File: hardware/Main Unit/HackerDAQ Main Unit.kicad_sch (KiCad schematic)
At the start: 10 parts, among them X2 8.192MHz

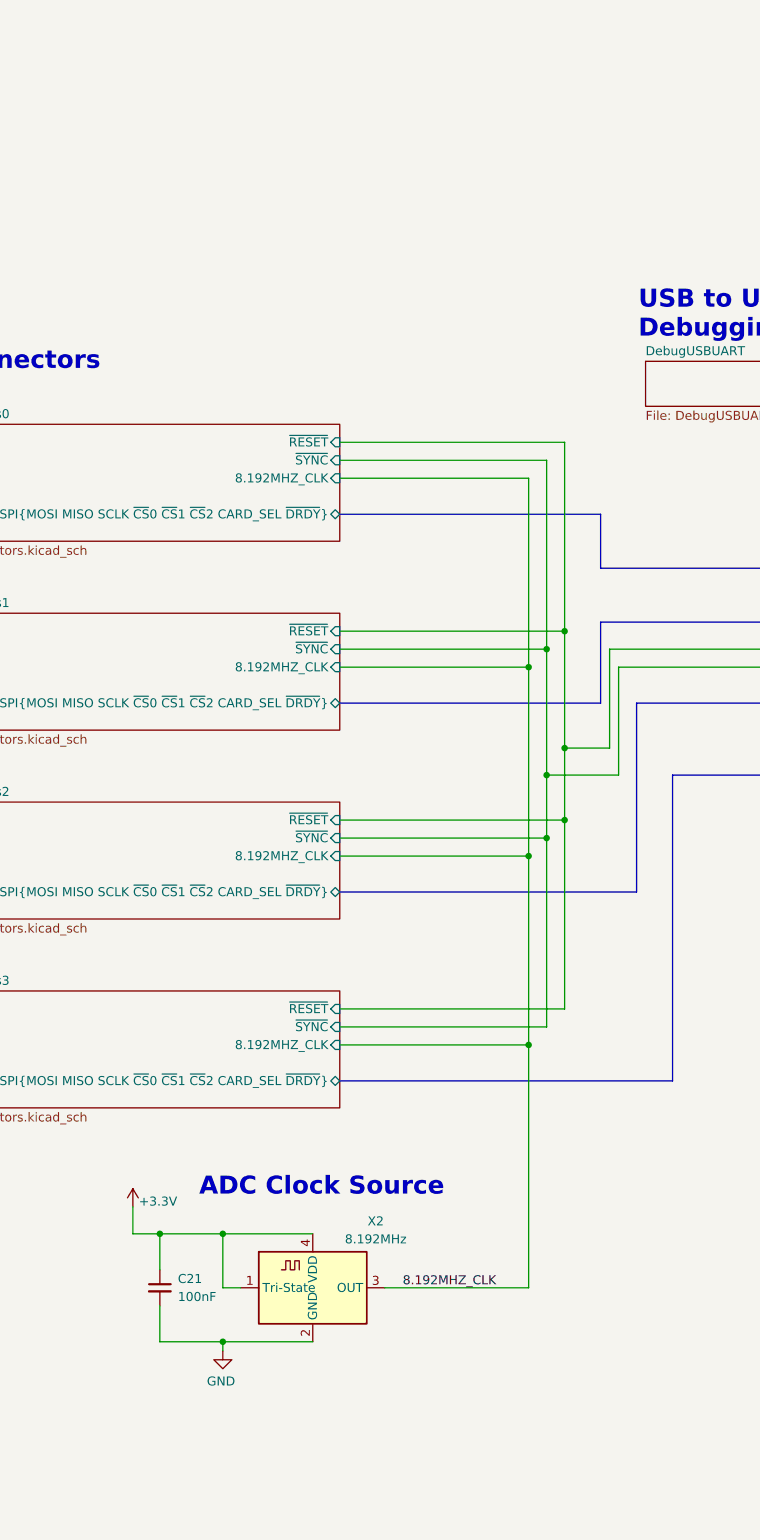
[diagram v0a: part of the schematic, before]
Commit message: Update main unit to KiCAD 10, add clock buffer
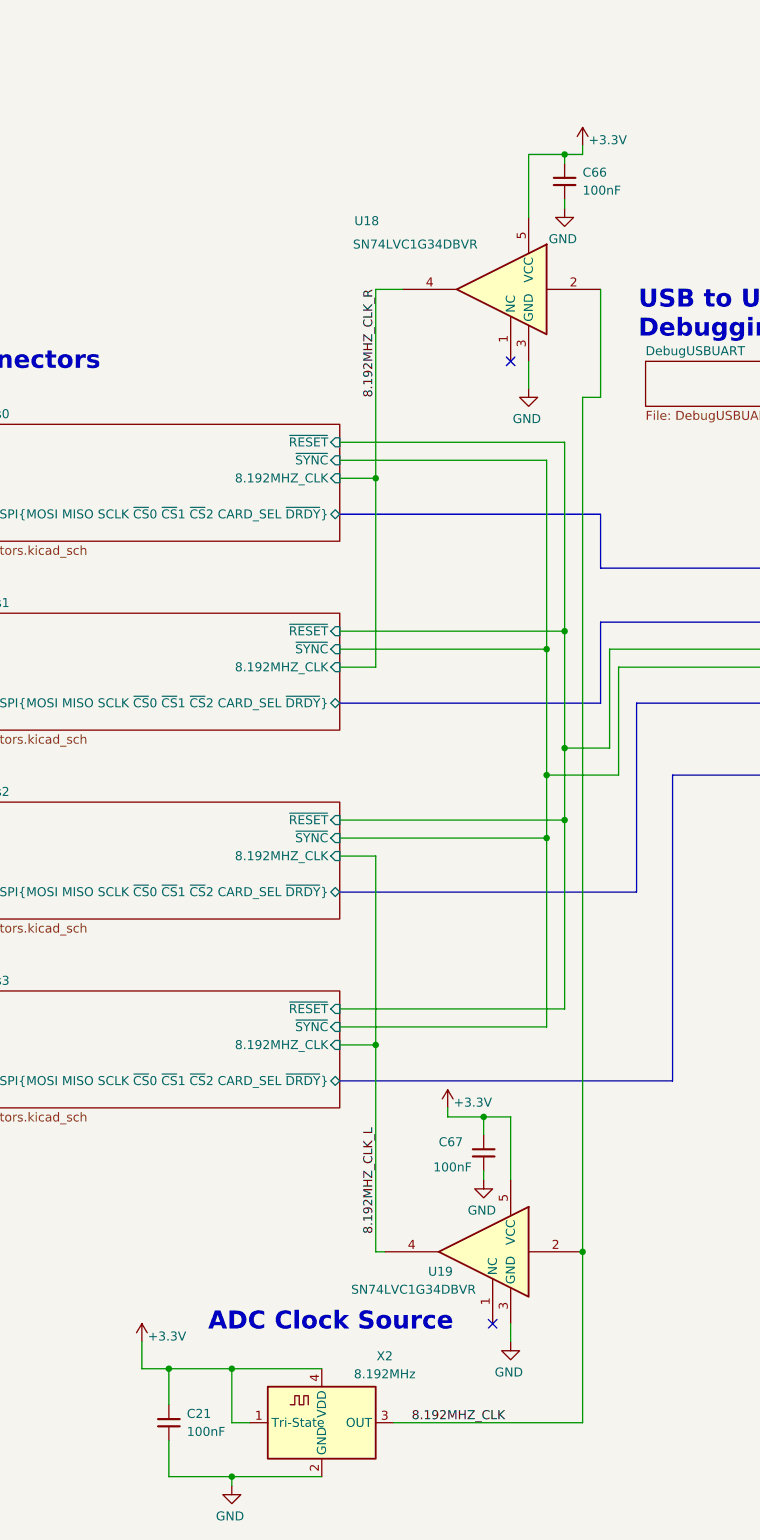
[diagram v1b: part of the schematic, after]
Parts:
- added C66, C67: 100nF, Capacitor_SMD:C_0603_1608Metric, symbol Device:C_Small
- added U18, U19: SN74LVC1G34DBVR, Package_TO_SOT_SMD:SOT-23-5, symbol 74xGxx:74LVC1G34
- LG1: value ~ -> (none)
- X2: footprint Project Library:Oscillator_SMD_ECS_2520MV-xxx-xx-4Pin_2.5x2.0mm_Fixed3DModel -> Oscillator:Oscillator_SMD_ECS_2520MV-xxx-xx-4Pin_2.5x2.0mm
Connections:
- net +3.3V: now also C66.1, C67.1, U18.5 (VCC), U19.5 (VCC)
- net 8.192MHZ_CLK: now also U18.2, U19.2
- net GND: now also C66.2, C67.2, U18.3 (GND), U19.3 (GND)
- new net 8.192MHZ_CLK_L: U19.4
- new net 8.192MHZ_CLK_R: U18.4
- no-connect marks 0 -> 2
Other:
- moved on the sheet: C21, X2

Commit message: Oops forgot to save
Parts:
- C22: renamed from C21; KiLib_Generator (none) -> Digi-Key
- H1, H2, H3, H4: KiLib_Generator (none) -> mounting_hardware/mounting_hole
- renumbered C66 to C12, C67 to C25, U18 to U4, U19 to U6
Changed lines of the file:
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@@
+			)
+		)
+		(property "KiLib_Generator" "mounting_hardware/mounting_hole"
+			(at 264.16 267.97 0)
+			(hide yes)
+			(show_name no)
+			(do_not_autoplace no)
+			(effects
+				(font
+					(size 1.27 1.27)
+				)
 			)
 		)
@@
 		(in_pos_files yes)
 		(dnp no)
-		(property "Reference" "U19"
+		(property "Reference" "U6"
 			(at 108.204 245.364 0)
 			(show_name no)
@@
 			(project "HackerDAQ Main Unit"
 				(path "/7d91f165-331a-4c48-9d02-ee2a0aa7e94a"
-					(reference "U19")
+					(reference "U6")
 					(unit 1)
 				)
@@
 		(in_pos_files yes)
 		(dnp no)
-		(property "Reference" "U18"
+		(property "Reference" "U4"
 			(at 97.79 97.028 0)
 			(show_name no)
@@
 			(project "HackerDAQ Main Unit"
 				(path "/7d91f165-331a-4c48-9d02-ee2a0aa7e94a"
-					(reference "U18")
+					(reference "U4")
 					(unit 1)
 				)
@@
 			)
 		)
+		(property "KiLib_Generator" "mounting_hardware/mounting_hole"
+			(at 254 267.97 0)
+			(hide yes)
+			(show_name no)
+			(do_not_autoplace no)
+			(effects
+				(font
+					(size 1.27 1.27)
+				)
+			)
+		)
 		(pin "1"
 		)
@@
 		(in_pos_files yes)
 		(dnp no)
-		(property "Reference" "C67"
+		(property "Reference" "C25"
 			(at 107.95 227.076 0)
 			(show_name no)
@@
 			(project "HackerDAQ Main Unit"
 				(path "/7d91f165-331a-4c48-9d02-ee2a0aa7e94a"
-					(reference "C67")
+					(reference "C25")
 					(unit 1)
 				)
@@
 		(dnp no)
 		(fields_autoplaced yes)
-		(property "Reference" "C66"
+		(property "Reference" "C12"
 			(at 128.27 90.1762 0)
 			(show_name no)
@@
 			(project "HackerDAQ Main Unit"
 				(path "/7d91f165-331a-4c48-9d02-ee2a0aa7e94a"
-					(reference "C66")
+					(reference "C12")
 					(unit 1)
 				)
@@
 		(dnp no)
 		(fields_autoplaced yes)
-		(property "Reference" "C21"
+		(property "Reference" "C22"
 			(at 72.39 265.4362 0)
 			(show_name no)
@@
 			)
 		)
+		(property "KiLib_Generator" "Digi-Key"
+			(at 69.85 266.7 0)
+			(hide yes)
+			(show_name no)
+			(do_not_autoplace no)
+			(effects
+				(font
+					(size 1.27 1.27)
+				)
+			)
+		)
 		(pin "1"
 		)
@@
 			(project "HackerDAQ Main Unit"
 				(path "/7d91f165-331a-4c48-9d02-ee2a0aa7e94a"
-					(reference "C21")
+					(reference "C22")
 					(unit 1)
 				)
@@
 			)
 		)
+		(property "KiLib_Generator" "mounting_hardware/mounting_hole"
+			(at 248.92 267.97 0)
+			(hide yes)
+			(show_name no)
+			(do_not_autoplace no)
+			(effects
+				(font
+					(size 1.27 1.27)
+				)
+			)
+		)
 		(pin "1"
 		)
@@
 			(at 259.08 267.97 0)
 			(hide yes)
+			(show_name no)
+			(do_not_autoplace no)
+			(effects
+				(font
+					(size 1.27 1.27)
+				)
+			)
+		)
+		(property "KiLib_Generator" "mounting_hardware/mounting_hole"
+			(at 259.08 267.97 0)
+			(hide yes)
